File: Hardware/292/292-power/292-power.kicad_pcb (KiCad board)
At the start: 2 copper layers, 24 x 50 mm, 77 parts, among them J1 Lock, J2 Battery, J3 Host, J4 ALT-HOST, J5 OTG, P1 HS, P2 PW, U1 W25X40CLSN, U2 RSH0056E, U3 RGE0024H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

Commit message: Clarifications for the board plan
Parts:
- J1: footprint Connector_JST:JST_ACH_BM03B-ACHSS-GAN-ETF_1x03-1MP_P1.20mm_Vertical -> Connector_JST:JST_SH_BM03B-SRSS-TB_1x03-1MP_P1.00mm_Vertical
- turned J1 to 180 degrees
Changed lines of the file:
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@@
     )
   )
-  (footprint "Connector_JST:JST_ACH_BM03B-ACHSS-GAN-ETF_1x03-1MP_P1.20mm_Vertical" (layer "F.Cu")
-    (at 71 141)
-    (descr "JST ACH series connector, BM03B-ACHSS-GAN-ETF (http://www.jst-mfg.com/product/pdf/eng/eACH.pdf), generated with kicad-footprint-generator")
-    (tags "connector JST ACH vertical")
+  (footprint "Connector_JST:JST_SH_BM03B-SRSS-TB_1x03-1MP_P1.00mm_Vertical" (layer "F.Cu")
+    (at 71 141 180)
+    (descr "JST SH series connector, BM03B-SRSS-TB (http://www.jst-mfg.com/product/pdf/eng/eSH.pdf), generated with kicad-footprint-generator")
+    (tags "connector JST SH side entry")
     (property "Sheetfile" "power-part.kicad_sch")
     (property "Sheetname" "Power Part")
     (attr smd)
-    (fp_text reference "J1" (at 0 -3.5) (layer "F.SilkS")
+    (fp_text reference "J1" (at 0 3) (layer "F.SilkS")
       (effects (font (size 1 1) (thickness 0.15)))
     )
-    (fp_text value "Lock" (at 0 3.5) (layer "F.Fab")
+    (fp_text value "Lock" (at 0 3.3) (layer "F.Fab")
       (effects (font (size 1 1) (thickness 0.15)))
     )
-    (fp_text user "${REFERENCE}" (at 0 0) (layer "F.Fab")
+    (fp_text user "${REFERENCE}" (at 0 -0.25) (layer "F.Fab")
       (effects (font (size 1 1) (thickness 0.15)))
     )
-    (fp_line (start -2.81 -2.11) (end -1.76 -2.11) (layer "F.SilkS") (width 0.12))
-    (fp_line (start -0.79 2.41) (end -0.39 1.91) (layer "F.SilkS") (width 0.12))
-    (fp_line (start -1.76 -2.11) (end -1.76 -2.3) (layer "F.SilkS") (width 0.12))
-    (fp_line (start 0.79 2.41) (end 1.74 2.41) (layer "F.SilkS") (width 0.12))
-    (fp_line (start -0.39 1.91) (end 0.39 1.91) (layer "F.SilkS") (width 0.12))
-    (fp_line (start -0.95 -3.153553) (end -1.45 -3.153553) (layer "F.SilkS") (width 0.12))
-    (fp_line (start -2.81 1.24) (end -2.81 -2.11) (layer "F.SilkS") (width 0.12))
-    (fp_line (start 0.39 1.91) (end 0.79 2.41) (layer "F.SilkS") (width 0.12))
-    (fp_line (start -1.2 -2.8) (end -0.95 -3.153553) (layer "F.SilkS") (width 0.12))
-    (fp_line (start -1.45 -3.153553) (end -1.2 -2.8) (layer "F.SilkS") (width 0.12))
-    (fp_line (start 2.81 1.24) (end 2.81 -2.11) (layer "F.SilkS") (width 0.12))
-    (fp_line (start -1.74 2.41) (end -0.79 2.41) (layer "F.SilkS") (width 0.12))
-    (fp_line (start 2.81 -2.11) (end 1.76 -2.11) (layer "F.SilkS") (width 0.12))
-    (fp_line (start -3.2 -2.8) (end -3.2 2.8) (layer "F.CrtYd") (width 0.05))
-    (fp_line (start 3.2 -2.8) (end -3.2 -2.8) (layer "F.CrtYd") (width 0.05))
-    (fp_line (start -3.2 2.8) (end 3.2 2.8) (layer "F.CrtYd") (width 0.05))
-    (fp_line (start 3.2 2.8) (end 3.2 -2.8) (layer "F.CrtYd") (width 0.05))
-    (fp_line (start -2.7 -2) (end -2.7 2.3) (layer "F.Fab") (width 0.1))
-    (fp_line (start -0.5 1.8) (end 0.5 1.8) (layer "F.Fab") (width 0.1))
-    (fp_line (start 2.7 -2) (end 2.7 2.3) (layer "F.Fab") (width 0.1))
-    (fp_line (start 0.9 2.3) (end 2.7 2.3) (layer "F.Fab") (width 0.1))
-    (fp_line (start -2.7 -2) (end 2.7 -2) (layer "F.Fab") (width 0.1))
-    (fp_line (start -2.7 2.3) (end -0.9 2.3) (layer "F.Fab") (width 0.1))
-    (fp_line (start 0.5 1.8) (end 0.9 2.3) (layer "F.Fab") (width 0.1))
-    (fp_line (start -1.7 -2) (end -1.2 -1.292893) (layer "F.Fab") (width 0.1))
-    (fp_line (start -1.2 -1.292893) (end -0.7 -2) (layer "F.Fab") (width 0.1))
-    (fp_line (start -0.9 2.3) (end -0.5 1.8) (layer "F.Fab") (width 0.1))
-    (pad "1" smd roundrect (at -1.2 -1.875) (size 0.6 0.85) (layers "F.Cu" "F.Paste" "F.Mask") (roundrect_rratio 0.25)
+    (fp_line (start -1.44 -2.01) (end 1.44 -2.01) (layer "F.SilkS") (width 0.12))
+    (fp_line (start 2.61 1.11) (end 1.56 1.11) (layer "F.SilkS") (width 0.12))
+    (fp_line (start 2.61 -0.04) (end 2.61 1.11) (layer "F.SilkS") (width 0.12))
+    (fp_line (start -2.61 -0.04) (end -2.61 1.11) (layer "F.SilkS") (width 0.12))
+    (fp_line (start -1.56 1.11) (end -1.56 2.1) (layer "F.SilkS") (width 0.12))
+    (fp_line (start -2.61 1.11) (end -1.56 1.11) (layer "F.SilkS") (width 0.12))
+    (fp_line (start -3.4 -2.6) (end -3.4 2.6) (layer "F.CrtYd") (width 0.05))
+    (fp_line (start -3.4 2.6) (end 3.4 2.6) (layer "F.CrtYd") (width 0.05))
+    (fp_line (start 3.4 2.6) (end 3.4 -2.6) (layer "F.CrtYd") (width 0.05))
+    (fp_line (start 3.4 -2.6) (end -3.4 -2.6) (layer "F.CrtYd") (width 0.05))
+    (fp_line (start -2.5 1) (end -2.5 -1.9) (layer "F.Fab") (width 0.1))
+    (fp_line (start -0.85 -1.55) (end -1.15 -1.55) (layer "F.Fab") (width 0.1))
+    (fp_line (start -2.5 -1.9) (end 2.5 -1.9) (layer "F.Fab") (width 0.1))
+    (fp_line (start 2.5 1) (end 2.5 -1.9) (layer "F.Fab") (width 0.1))
+    (fp_line (start -1.5 1) (end -1 0.292893) (layer "F.Fab") (width 0.1))
+    (fp_line (start -2.5 1) (end 2.5 1) (layer "F.Fab") (width 0.1))
+    (fp_line (start -0.15 -1.55) (end -0.15 -0.95) (layer "F.Fab") (width 0.1))
+    (fp_line (start -1.15 -1.55) (end -1.15 -0.95) (layer "F.Fab") (width 0.1))
+    (fp_line (start -1 0.292893) (end -0.5 1) (layer "F.Fab") (width 0.1))
+    (fp_line (start 0.15 -1.55) (end -0.15 -1.55) (layer "F.Fab") (width 0.1))
+    (fp_line (start 0.85 -0.95) (end 1.15 -0.95) (layer "F.Fab") (width 0.1))
+    (fp_line (start 1.15 -0.95) (end 1.15 -1.55) (layer "F.Fab") (width 0.1))
+    (fp_line (start -0.85 -0.95) (end -0.85 -1.55) (layer "F.Fab") (width 0.1))
+    (fp_line (start 0.85 -1.55) (end 0.85 -0.95) (layer "F.Fab") (width 0.1))
+    (fp_line (start -0.15 -0.95) (end 0.15 -0.95) (layer "F.Fab") (width 0.1))
+    (fp_line (start 1.15 -1.55) (end 0.85 -1.55) (layer "F.Fab") (width 0.1))
+    (fp_line (start 0.15 -0.95) (end 0.15 -1.55) (layer "F.Fab") (width 0.1))
+    (fp_line (start -1.15 -0.95) (end -0.85 -0.95) (layer "F.Fab") (width 0.1))
+    (pad "1" smd roundrect (at -1 1.325 180) (size 0.6 1.55) (layers "F.Cu" "F.Paste" "F.Mask") (roundrect_rratio 0.25)
       (net 31 "/Power Part/LOCK_BTN") (pinfunction "Pin_1") (pintype "passive"))
-    (pad "2" smd roundrect (at 0 -1.875) (size 0.6 0.85) (layers "F.Cu" "F.Paste" "F.Mask") (roundrect_rratio 0.25)
+    (pad "2" smd roundrect (at 0 1.325 180) (size 0.6 1.55) (layers "F.Cu" "F.Paste" "F.Mask") (roundrect_rratio 0.25)
       (net 32 "/Power Part/PD_LDO_3V3") (pinfunction "Pin_2") (pintype "passive"))
-    (pad "3" smd roundrect (at 1.2 -1.875) (size 0.6 0.85) (layers "F.Cu" "F.Paste" "F.Mask") (roundrect_rratio 0.25)
+    (pad "3" smd roundrect (at 1 1.325 180) (size 0.6 1.55) (layers "F.Cu" "F.Paste" "F.Mask") (roundrect_rratio 0.25)
       (net 33 "/Power Part/SHUTDOWN_BTN") (pinfunction "Pin_3") (pintype "passive"))
-    (pad "MP" smd roundrect (at 2.35 1.9) (size 0.7 0.8) (layers "F.Cu" "F.Paste" "F.Mask") (roundrect_rratio 0.25))
-    (pad "MP" smd roundrect (at -2.35 1.9) (size 0.7 0.8) (layers "F.Cu" "F.Paste" "F.Mask") (roundrect_rratio 0.25))
-    (model "${KICAD6_3DMODEL_DIR}/Connector_JST.3dshapes/JST_ACH_BM03B-ACHSS-GAN-ETF_1x03-1MP_P1.20mm_Vertical.wrl"
+    (pad "MP" smd roundrect (at 2.3 -1.2 180) (size 1.2 1.8) (layers "F.Cu" "F.Paste" "F.Mask") (roundrect_rratio 0.208333))
+    (pad "MP" smd roundrect (at -2.3 -1.2 180) (size 1.2 1.8) (layers "F.Cu" "F.Paste" "F.Mask") (roundrect_rratio 0.208333))
+    (model "${KICAD6_3DMODEL_DIR}/Connector_JST.3dshapes/JST_SH_BM03B-SRSS-TB_1x03-1MP_P1.00mm_Vertical.wrl"
       (offset (xyz 0 0 0))
       (scale (xyz 1 1 1))
@@
     (fp_arc (start 3.925 -0.25) (mid 4.066421 -0.191421) (end 4.125 -0.05) (layer "Edge.Cuts") (width 0.01))
     (fp_arc (start 3.625 0.25) (mid 3.483579 0.191421) (end 3.425 0.05) (layer "Edge.Cuts") (width 0.01))
-    (fp_arc (start 4.41927 0.675741) (mid 4.521786 0.923226) (end 4.419271 1.17071) (layer "Edge.Cuts") (width 0.01))
+    (fp_arc (start 4.41927 0.675741) (mid 4.521789 0.923226) (end 4.419271 1.17071) (layer "Edge.Cuts") (width 0.01))
     (fp_arc (start -4.41926 1.17071) (mid -4.521773 0.923222) (end -4.41926 0.675734) (layer "Edge.Cuts") (width 0.01))
     (fp_arc (start -4.125 -0.05) (mid -4.066421 -0.191421) (end -3.925 -0.25) (layer "Edge.Cuts") (width 0.01))
@@
     (fp_arc (start -3.925 0.25) (mid -4.066421 0.191421) (end -4.125 0.05) (layer "Edge.Cuts") (width 0.01))
     (fp_arc (start 3.92429 0.675741) (mid 4.17178 0.573227) (end 4.41927 0.675741) (layer "Edge.Cuts") (width 0.01))
-    (fp_arc (start 4.41927 -1.17071) (mid 4.52178 -0.923227) (end 4.41927 -0.675742) (layer "Edge.Cuts") (width 0.01))
+    (fp_arc (start 4.41927 -1.17071) (mid 4.521777 -0.923227) (end 4.41927 -0.675742) (layer "Edge.Cuts") (width 0.01))
     (fp_arc (start 4.125 0.05) (mid 4.066421 0.191421) (end 3.925 0.25) (layer "Edge.Cuts") (width 0.01))
     (fp_arc (start 4.41927 -0.675741) (mid 4.17178 -0.573227) (end 3.92429 -0.675741) (layer "Edge.Cuts") (width 0.01))
@@
     (fp_arc (start -3.57073 -1.52426) (mid -3.468218 -1.276775) (end -3.57073 -1.02929) (layer "Edge.Cuts") (width 0.01))
     (fp_arc (start -3.425 0.05) (mid -3.483579 0.191421) (end -3.625 0.25) (layer "Edge.Cuts") (width 0.01))
-    (fp_arc (start 4.41927 -1.17071) (mid 4.52178 -0.923227) (end 4.41927 -0.675742) (layer "Edge.Cuts") (width 0.01))
+    (fp_arc (start 4.41927 -1.17071) (mid 4.521777 -0.923227) (end 4.41927 -0.675742) (layer "Edge.Cuts") (width 0.01))
     (fp_arc (start 4.41927 -0.675741) (mid 4.17178 -0.573227) (end 3.92429 -0.675741) (layer "Edge.Cuts") (width 0.01))
     (fp_arc (start -3.625 -0.25) (mid -3.483579 -0.191421) (end -3.425 -0.05) (layer "Edge.Cuts") (width 0.01))
-    (fp_arc (start 4.41927 0.675741) (mid 4.521786 0.923226) (end 4.419271 1.17071) (layer "Edge.Cuts") (width 0.01))
+    (fp_arc (start 4.41927 0.675741) (mid 4.521789 0.923226) (end 4.419271 1.17071) (layer "Edge.Cuts") (width 0.01))
     (fp_arc (start 4.125 0.05) (mid 4.066421 0.191421) (end 3.925 0.25) (layer "Edge.Cuts") (width 0.01))
     (fp_arc (start 3.57074 1.52427) (mid 3.468226 1.27678) (end 3.57074 1.02929) (layer "Edge.Cuts") (width 0.01))

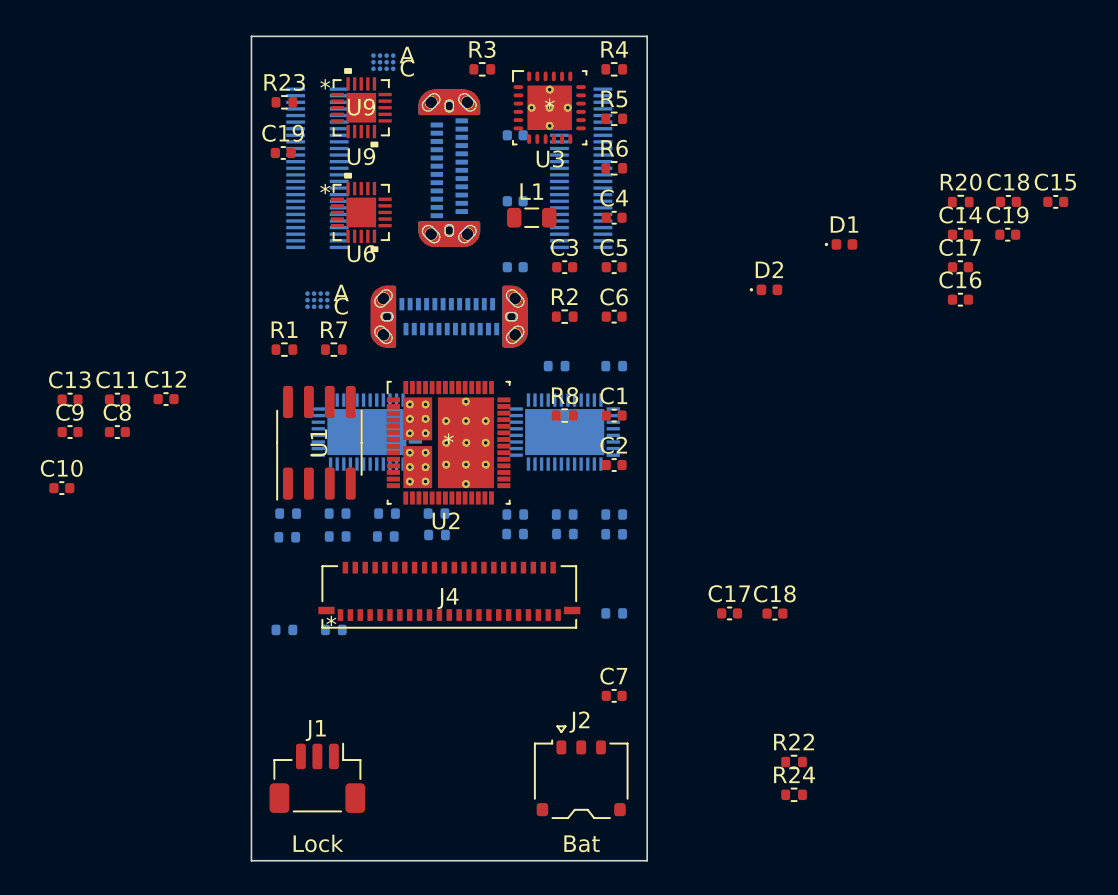
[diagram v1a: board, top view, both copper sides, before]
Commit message: Moved power/lock connectors
Need space to place batteries
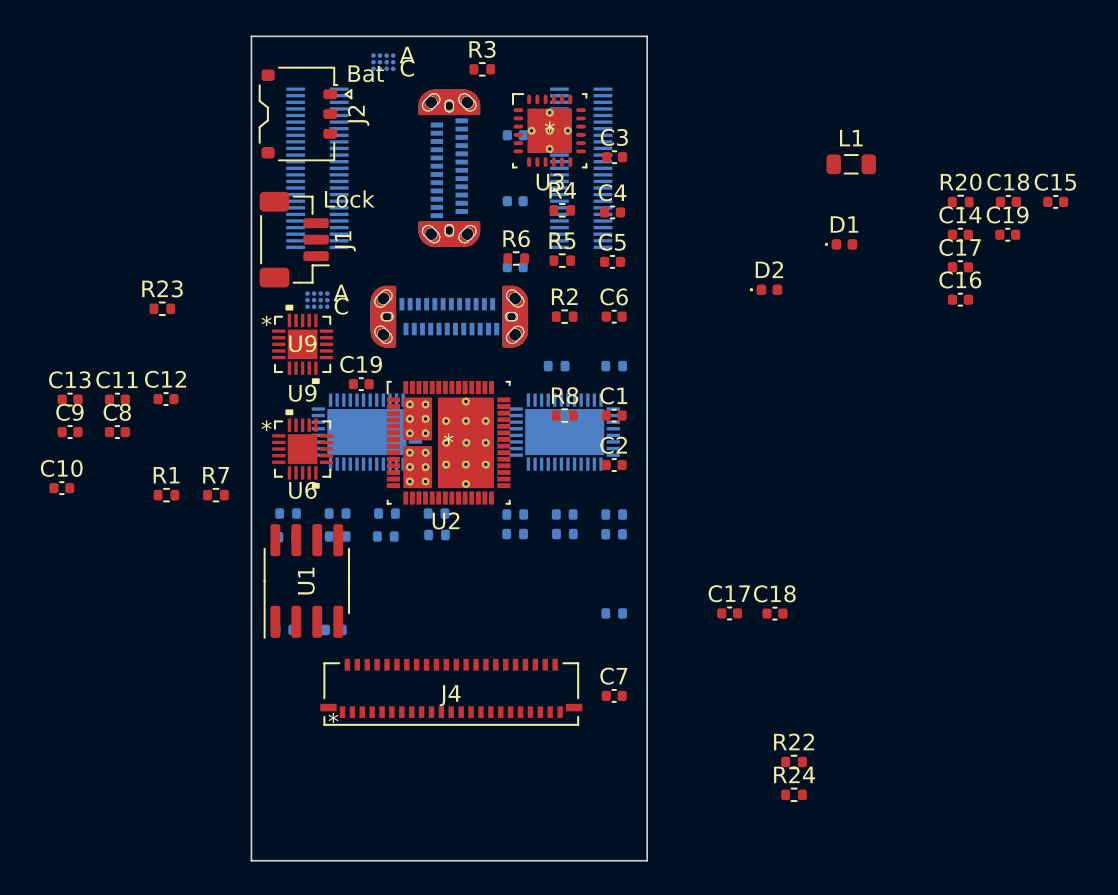
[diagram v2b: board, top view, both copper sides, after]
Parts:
- moved J2 43.8 mm to (69.9, 100.7), turned to -90 degrees
- moved J1 32.7 mm to (69.6, 108.3), turned to 90 degrees
- moved L1 19.6 mm to (103.4, 103.8)
- moved C19 14.8 mm to (73.7, 117.1)
- moved U6 14.8 mm to (70.1, 121.0)
- moved U9 14.8 mm to (70.1, 114.7)
- moved R23 14.5 mm to (61.6, 112.5)
- moved R1 11.4 mm to (61.8, 123.8)
- moved R7 11.4 mm to (64.8, 123.8)
- moved R5 9.16 mm to (85.9, 109.6)
- moved R4 9.11 mm to (85.9, 106.6)
- moved U1 8.42 mm to (70.4, 129.0)
- moved R6 8.08 mm to (83.1, 109.5)
- moved C3 7.32 mm to (89.0, 103.3)
- moved J4 5.89 mm to (79.1, 135.9)
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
